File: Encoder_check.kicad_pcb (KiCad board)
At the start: 2 copper layers, 17.8 x 43.2 mm, 18 parts, among them J1 Conn_01x08, J2 Conn_01x06, P1 Digital, P2 Analog, P3 CONN_01X01, P4 CONN_01X01, P5 CONN_01X01, P6 CONN_01X01, U1 AM26LV32xD, U2 ST490AB

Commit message: AW
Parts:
- removed P3, P4, P5, P6: CONN_01X01, Socket_Arduino_Nano:1pin_Nano
- added C10: 10n, Capacitor_SMD:C_0603_1608Metric, F.Cu at (173.4, 63.7)
- added C11: DNP, Capacitor_SMD:C_0603_1608Metric, F.Cu at (173.4, 67.0)
- added C12: C, Capacitor_SMD:C_1206_3216Metric, B.Cu at (135.2, 85.1)
- added C13: 0.1u, Capacitor_SMD:C_0603_1608Metric, B.Cu at (139.9, 69.3)
- added C14: 3.3u, Capacitor_SMD:C_0805_2012Metric, B.Cu at (154.7, 55.4)
- added C15: 0.1u, Capacitor_SMD:C_0603_1608Metric, B.Cu at (148.5, 103.0)
- added C16: 1u, Capacitor_SMD:C_0805_2012Metric, B.Cu at (142.7, 104.8)
- added C17: C, Capacitor_SMD:C_0603_1608Metric, B.Cu at (151.0, 103.0)
- added C3: 220p, Capacitor_SMD:C_0603_1608Metric, B.Cu at (184.6, 75.1)
- added C4: 0.1u, Capacitor_SMD:C_0603_1608Metric, F.Cu at (184.8, 74.6)
- added C5: 220p, Capacitor_SMD:C_0603_1608Metric, B.Cu at (182.2, 98.4)
- added C6: 220p, Capacitor_SMD:C_0603_1608Metric, B.Cu at (182.2, 93.4)
- added C7: 0.1u, Capacitor_SMD:C_0603_1608Metric, B.Cu at (178.3, 106.3)
- added C8: C, Capacitor_SMD:C_0603_1608Metric, F.Cu at (170.6, 60.3)
- added C9: DNP, Capacitor_SMD:C_0603_1608Metric, F.Cu at (173.4, 60.4)
- added D10: LED, LED_SMD:LED_0603_1608Metric, F.Cu at (132.9, 61.4)
- added D11: LED, LED_SMD:LED_0603_1608Metric, F.Cu at (163.7, 114.6)
- added D4: D_TVS_x2_AAC, Package_TO_SOT_SMD:SOT-23, F.Cu at (175.9, 63.7)
- added D5: SK6805, LED_SMD:LED_SK6805_PLCC4_2.4x2.7mm_P1.3mm, F.Cu at (173.0, 115.0)
- added D6: SK6805, LED_SMD:LED_SK6805_PLCC4_2.4x2.7mm_P1.3mm, F.Cu at (178.2, 115.0)
- added D7: SK6805, LED_SMD:LED_SK6805_PLCC4_2.4x2.7mm_P1.3mm, F.Cu at (183.4, 115.0)
- added D8: D, Diode_SMD:D_SOD-523, B.Cu at (138.7, 91.4)
- added D9: D, Diode_SMD:D_SOD-523, B.Cu at (138.6, 87.0)
- added H1: MountingHole, MountingHole:MountingHole_3.2mm_M3, F.Cu at (132.2, 50.6)
- added H2: MountingHole, MountingHole:MountingHole_3.2mm_M3, F.Cu at (132.2, 115.6)
- added H3: MountingHole, MountingHole:MountingHole_3.2mm_M3, F.Cu at (190.2, 50.6)
- added H4: MountingHole, MountingHole:MountingHole_3.2mm_M3, F.Cu at (190.2, 115.6)
- added J3: Conn_01x04, Connector_JST:JST_EH_S4B-EH_1x04_P2.50mm_Horizontal, F.Cu at (136.1, 78.9)
- added J4: Screw_Terminal_01x06, TerminalBlock_TE-Connectivity:TerminalBlock_TE_282834-6_1x06_P2.54mm_Horizontal, F.Cu at (132.7, 83.9)
- added J5: Conn_01x02, Connector_PinHeader_2.54mm:PinHeader_1x02_P2.54mm_Vertical, F.Cu at (136.3, 66.9)
- added J6: Screw_Terminal_01x02, TerminalBlock_Phoenix:TerminalBlock_Phoenix_MKDS-1,5-2-5.08_1x02_P5.08mm_Horizontal, F.Cu at (188.0, 66.3)
- added J7: Barrel_Jack_Switch, Connector_BarrelJack:BarrelJack_Horizontal, F.Cu at (140.6, 61.6)
- added J8: Screw_Terminal_01x02, TerminalBlock_Phoenix:TerminalBlock_Phoenix_MKDS-1,5-2-5.08_1x02_P5.08mm_Horizontal, F.Cu at (134.0, 103.9)
- added J9: Screw_Terminal_01x04, TerminalBlock_TE-Connectivity:TerminalBlock_TE_282834-4_1x04_P2.54mm_Horizontal, F.Cu at (141.7, 115.1)
- added L1: L, Inductor_SMD:L_0603_1608Metric, F.Cu at (174.9, 67.0)
- added L2: L, Inductor_SMD:L_0603_1608Metric, F.Cu at (174.9, 60.4)
- added L3: L, Inductor_SMD:L_0603_1608Metric, B.Cu at (133.0, 81.8)
- added L4: L, Inductor_SMD:L_1210_3225Metric, B.Cu at (143.3, 108.9)
- added Q1: BSS138, Package_TO_SOT_SMD:SOT-23, B.Cu at (173.4, 115.0)
- added Q2: BSS138, Package_TO_SOT_SMD:SOT-23, B.Cu at (179.5, 77.1)
- added R10: 20k, Resistor_SMD:R_0603_1608Metric, B.Cu at (182.2, 94.8)
- added R11: 10k, Resistor_SMD:R_0603_1608Metric, B.Cu at (135.6, 88.5)
- added R12: 10k, Resistor_SMD:R_0603_1608Metric, B.Cu at (135.6, 89.9)
- added R13: 1k, Resistor_SMD:R_0603_1608Metric, B.Cu at (135.6, 92.6)
- added R14: 10k, Resistor_SMD:R_0603_1608Metric, B.Cu at (138.6, 88.5)
- added R15: 10k, Resistor_SMD:R_0603_1608Metric, B.Cu at (138.6, 89.9)
- added R16: R, Resistor_SMD:R_0603_1608Metric, B.Cu at (133.8, 69.9)
- added R17: 10k, Resistor_SMD:R_0603_1608Metric, B.Cu at (179.3, 74.3)
- added R18: 1k, Resistor_SMD:R_0603_1608Metric, B.Cu at (182.0, 77.2)
- added R19: 0.05, Inductor_SMD:L_0805_2012Metric, B.Cu at (145.8, 105.6)
- added R20: 0, Inductor_SMD:L_0805_2012Metric, B.Cu at (139.6, 106.0)
- added R21: R, Resistor_SMD:R_1206_3216Metric, B.Cu at (138.6, 108.9)
- added R22: R, Inductor_SMD:L_0603_1608Metric, B.Cu at (151.0, 106.0)
- added R23: 10k, Resistor_SMD:R_0603_1608Metric, B.Cu at (171.0, 115.0)
- added R24: 10k, Resistor_SMD:R_0603_1608Metric, B.Cu at (175.9, 115.0)
- added R25: 1k, Resistor_SMD:R_0603_1608Metric, B.Cu at (146.7, 112.9)
- added R26: R, Resistor_SMD:R_0603_1608Metric, B.Cu at (161.9, 112.2)
- added R27: R, Resistor_SMD:R_0603_1608Metric, F.Cu at (132.9, 58.3)
- added R28: R, Resistor_SMD:R_0603_1608Metric, F.Cu at (163.7, 113.0)
- added R4: 4.7k, Resistor_SMD:R_0603_1608Metric, B.Cu at (187.0, 78.7)
- added R5: 4.7k, Resistor_SMD:R_0603_1608Metric, B.Cu at (187.0, 80.1)
- added R6: 150, Resistor_SMD:R_0603_1608Metric, B.Cu at (187.0, 77.3)
- added R7: 150, Resistor_SMD:R_0603_1608Metric, B.Cu at (187.0, 75.9)
- added R8: 20k, Resistor_SMD:R_0603_1608Metric, B.Cu at (182.2, 104.8)
- added R9: 20k, Resistor_SMD:R_0603_1608Metric, B.Cu at (182.2, 99.8)
- added RN1: R_Pack02, Resistor_SMD:R_Array_Concave_2x0603, B.Cu at (183.0, 106.6)
- added RN2: R_Pack02, Resistor_SMD:R_Array_Concave_2x0603, B.Cu at (183.0, 101.6)
- added RN3: R_Pack02, Resistor_SMD:R_Array_Concave_2x0603, B.Cu at (183.0, 96.6)
- added RN4: R_Pack02, Resistor_SMD:R_Array_Concave_2x0603, F.Cu at (181.5, 104.3)
- added RN5: R_Pack02, Resistor_SMD:R_Array_Concave_2x0603, F.Cu at (181.5, 99.3)
- added RN6: R_Pack02, Resistor_SMD:R_Array_Concave_2x0603, F.Cu at (181.5, 94.3)
- added TC1: Thermocouple_PCB, Connector_Omega:Omega_PCC-SMP_1x2_P13.70mm_Horizontal, F.Cu at (174.9, 63.7)
- added U3: AM26LV32xD, Package_SO:SOIC-16_3.9x9.9mm_P1.27mm, B.Cu at (177.0, 100.4)
- added U4: SP3481CN, Package_SO:SOIC-8_3.9x4.9mm_P1.27mm, B.Cu at (141.1, 72.7)
- added U5: M78AR05-1, Converter_DCDC_my:Converter_DCDC_MINIMAX_M78AR05-1_THT, F.Cu at (152.2, 59.1)
- added U6: INA180A, Package_TO_SOT_SMD:SOT-23-5, B.Cu at (148.5, 105.6)
- added U7: A4953_LJ, Package_SO:SOIC-8-1EP_3.9x4.9mm_P1.27mm_EP2.41x3.3mm, B.Cu at (139.0, 101.3)
- added U8: TLP785, Package_DIP:DIP-4_W7.62mm, F.Cu at (152.4, 112.9)
- C1, C2: value C -> 220p; moved to B.Cu
- J1: value Conn_01x08 -> Conn_01x10; footprint TerminalBlock_TE-Connectivity:TerminalBlock_TE_282834-8_1x08_P2.54mm_Horizontal -> Connector_Multicomp:Multicomp_MC9A12-1034_2x05_P2.54mm_Vertical
- R1, R2, R3: moved to B.Cu
- U1: value AM26LV32xD -> MAX31855KASA; footprint Package_SO:SOIC-16_3.9x9.9mm_P1.27mm -> Package_SO:SOIC-8_3.9x4.9mm_P1.27mm; moved to F.Cu
- U2: value ST490AB -> ADM1491EBR; footprint Package_SO:SO-8_3.9x4.9mm_P1.27mm -> Package_SO:SOIC-14_3.9x8.7mm_P1.27mm
- moved J1 85.1 mm to (187.1, 96.0)
- moved J2 83.0 mm to (189.7, 88.1), turned to 90 degrees
- moved U2 68.1 mm to (180.4, 79.3)
- moved C2 65.8 mm to (184.6, 78.1), turned to 270 degrees
- moved D2 64.6 mm to (176.8, 95.5), turned to 270 degrees
- moved D1 63.5 mm to (179.3, 95.5), turned to 270 degrees
- moved R2 61.2 mm to (178.4, 92.8), turned to 90 degrees
- moved R1 59.2 mm to (179.9, 92.8), turned to 90 degrees
- moved C1 57.9 mm to (182.2, 103.4)
- moved D3 57.9 mm to (174.2, 95.5), turned to 270 degrees
- moved R3 57.1 mm to (176.9, 92.8), turned to 90 degrees
- moved U1 51.8 mm to (168.9, 63.7), turned to 180 degrees
- moved P1 16.1 mm to (155.5, 70.2)
- moved P2 16.1 mm to (170.8, 70.2)
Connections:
- C1 pad 1: +5V -> /inc_encoder/I_-
- C2 pad 1: +5V -> /ssi_encoder/Dout_-
- J1 pad 1: GND -> (no net)
- J1 pad 2: +5V -> GND
- J1 pad 3: Net-(J1-Pad3) -> +5V
- J1 pad 4: Net-(J1-Pad4) -> (no net)
- J1 pad 5: Net-(J1-Pad5) -> /inc_encoder/A+
- J1 pad 6: Net-(J1-Pad6) -> /inc_encoder/A-
- J1 pad 7: Net-(J1-Pad7) -> /inc_encoder/B+
- J1 pad 8: Net-(J1-Pad8) -> /inc_encoder/B-
- J2 pad 3: Net-(J2-Pad3) -> /ssi_encoder/C_-
- J2 pad 4: Net-(J2-Pad4) -> /ssi_encoder/C_+
- J2 pad 5: Net-(J2-Pad5) -> /ssi_encoder/D_-
- J2 pad 6: Net-(J2-Pad6) -> /ssi_encoder/D_+
- P1 pad 1: (no net) -> /1(Tx)
- P1 pad 12: (no net) -> /9(**)
- P1 pad 13: (no net) -> /10(**/SS)
- P1 pad 14: (no net) -> /11(**/MOSI)
- P1 pad 15: (no net) -> /12(MISO)
- P1 pad 2: (no net) -> /0(Rx)
- P1 pad 5: (no net) -> /2
- P1 pad 7: (no net) -> /4
- P1 pad 9: (no net) -> /6(**)
- P2 pad 14: (no net) -> +3V3
- P2 pad 6: (no net) -> /A6
- P2 pad 9: (no net) -> /A3
- U1 pad 1: Net-(J1-Pad4) -> GND
- U1 pad 2: Net-(J1-Pad3) -> Net-(C10-Pad2)
- U1 pad 3: /A0 -> Net-(C10-Pad1)
- U1 pad 4: /3(**) -> +3V3
- U1 pad 5: /A1 -> /A4
- U1 pad 6: Net-(J1-Pad5) -> /A3
- U1 pad 7: Net-(J1-Pad6) -> /12(MISO)
- U1 pad 8: GND -> (no net)
- U2 pad 1: +5V -> (no net)
- U2 pad 2: /A5 -> /12(MISO)
- U2 pad 3: /A4 -> Net-(Q2-Pad3)
- U2 pad 4: GND -> /3(**)
- U2 pad 5: Net-(J2-Pad3) -> /A4
- U2 pad 6: Net-(J2-Pad4) -> GND
- U2 pad 7: Net-(J2-Pad6) -> GND
- U2 pad 8: Net-(J2-Pad5) -> (no net)
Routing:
- net GND: track 0.00 -> 382.2 mm, vias 0 -> 8
- net +5V: track 0.00 -> 217.4 mm, vias 0 -> 5
- net +3V3: track 0.00 -> 162.7 mm, vias 0 -> 6
- net +24V: track 0.00 -> 88.2 mm, vias 0 -> 2
- net /12(MISO): track 0.00 -> 61.5 mm, vias 0 -> 2
- net /A4: track 0.00 -> 43.4 mm, vias 0 -> 2
- net /1(Tx): track 0.00 -> 41.1 mm, vias 0 -> 1
- net /A5: track 0.00 -> 39.2 mm, vias 0 -> 1
- net /A6: track 0.00 -> 31.7 mm, vias 0 -> 1
- net /A3: track 0.00 -> 31.3 mm
- net /3(**): track 0.00 -> 30.1 mm, vias 0 -> 2
- net /5(**): track 0.00 -> 29.2 mm, vias 0 -> 1
- net /4: track 0.00 -> 29.1 mm
- net /11(**/MOSI): track 0.00 -> 21.4 mm
- net /6(**): track 0.00 -> 21.0 mm
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- added copper zone on B.Cu, net GND
- added copper zone on F.Cu, net GND
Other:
- board size 17.8 x 43.2 mm -> 64 x 71 mm
- net class Default: clearance 0.2 -> 0.199; trace_width 0.25 -> 0.2
- rule trace_clearance: 0.2 -> 0.199
- rule trace_min: 0.2 -> 0.199
- board text added: "24V"
- board text added: "5V"
- board text added: "A"
- board text added: "Absolute Encoder"
- board text added: "B"
- board text added: "Brake"
- board text added: "D+"
- board text added: "D-"
- board text added: "GND"
- board text added: "I"
- board text added: "PULSE_OUT+"
- board text added: "PULSE_OUT-"
- board text added: "PWR+(24V)"
- board text added: "PWR-(0V)"
- board text added: "RS485"
- board text added: "SIG_GND"
- board text added: "SIG_OUT"
- board text added: "STO"
- board text added: "Term"
- board text added: "UTMII"

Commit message: これで発注
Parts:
- C16: footprint Capacitor_SMD:C_0805_2012Metric -> Capacitor_SMD:C_1206_3216Metric
- R28: moved to B.Cu
- moved R27 13.5 mm to (144.8, 64.6), turned to 0 degrees
- moved D10 9.27 mm to (141.6, 64.6), turned to 180 degrees
- moved Q2 7.00 mm to (175.3, 82.7)
- moved R17 6.68 mm to (175.1, 79.5)
- moved C4 5.26 mm to (179.9, 76.5), turned to 180 degrees
- moved R18 5.16 mm to (177.8, 80.2)
- moved C16 4.52 mm to (140.8, 100.7), turned to 90 degrees
- moved R19 4.44 mm to (143.2, 102.0)
- moved U6 4.44 mm to (145.9, 102.0)
- moved C15 4.44 mm to (145.9, 99.4)
- moved C17 4.44 mm to (148.4, 99.4)
- moved R22 4.44 mm to (148.4, 102.4)
- moved R26 3.69 mm to (165.0, 114.2), turned to 180 degrees
- moved R28 3.45 mm to (165.0, 116.2)
- moved U2 3.33 mm to (178.2, 81.8)
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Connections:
- J9 pad 1: +5V -> GND
- J9 pad 4: GND -> +5V
- R25 pad 2: Net-(J9-Pad2) -> Net-(J9-Pad3)
- U8 pad 2: Net-(J9-Pad3) -> Net-(J9-Pad2)
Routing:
- net +24V: track 88.2 -> 115.2 mm, vias 2 -> 4
- net GND: track 382.2 -> 371.0 mm, vias 8 -> 152
- net Net-(J9-Pad2): track 4.19 -> 13.7 mm
- net /5(**): track 29.2 -> 37.0 mm
- net /10(**/SS): track 19.7 -> 25.6 mm, vias 1 -> 0
- net /3(**): track 30.1 -> 24.2 mm
- net +5V: track 217.4 -> 223.2 mm, vias 5 -> 8
- net /A1: track 11.3 -> 16.4 mm
- net Net-(J9-Pad3): track 7.17 -> 2.21 mm
- net /A4: track 43.4 -> 38.6 mm, vias 2 -> 1
- net /11(**/MOSI): track 21.4 -> 24.9 mm
- net /12(MISO): track 61.5 -> 58.5 mm
- net /9(**): track 17.4 -> 20.1 mm
- net +3V3: track 162.7 -> 160.1 mm, vias 6 -> 5
- net /ssi_encoder/Dout_-: track 6.46 -> 8.33 mm
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- added copper zone on F.Cu, net /thermocouple/T+
- added copper zone on F.Cu, net /thermocouple/T-
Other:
- board text added: "C+"
- board text added: "C-"
- board text removed: "Absolute Encoder"

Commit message: 見つけた設計ミスを全部反映
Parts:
- removed R1, R2, R3: R, Resistor_SMD:R_0603_1608Metric
- added L5: L, Inductor_SMD:L_0603_1608Metric, F.Cu at (171.3, 58.0)
- added L6: L, Inductor_SMD:L_0603_1608Metric, B.Cu at (146.6, 97.1)
- added R29: 10k, Resistor_SMD:R_0603_1608Metric, F.Cu at (182.6, 94.5)
- added R30: 20k, Resistor_SMD:R_0603_1608Metric, F.Cu at (181.0, 94.5)
- C17, C8: value C -> 0.1u
- J1: value Conn_01x10 -> Conn_02x05_Odd_Even
- J2: value Conn_01x06 -> Screw_Terminal_01x06
- R16: value R -> 120
- R27: value R -> 20k
- R4: value 4.7k -> 10k; moved to F.Cu
- R5: value 4.7k -> 20k; moved to F.Cu
- R6: value 150 -> 10k; moved to F.Cu
- R7: value 150 -> 20k; moved to F.Cu
- RN1, RN2, RN3: value R_Pack02 -> 150
- RN4: value R_Pack02 -> 4.7k; moved to B.Cu
- RN5: value R_Pack02 -> 150; moved to B.Cu
- RN6: value R_Pack02 -> 1k; footprint Resistor_SMD:R_Array_Concave_2x0603 -> Resistor_SMD:R_Array_Concave_4x0603; moved to B.Cu
- U2: value ADM1491EBR -> ISL83491
- U4: value SP3481CN -> ST485BDR
- moved R5 26.0 mm to (181.0, 104.5), turned to 270 degrees
- moved RN4 25.7 mm to (184.9, 78.8), turned to 180 degrees
- moved R4 24.3 mm to (182.6, 104.5), turned to 270 degrees
- moved R7 23.9 mm to (181.0, 99.5), turned to 270 degrees
- moved RN5 23.0 mm to (184.9, 76.6), turned to 0 degrees
- moved R6 22.3 mm to (182.6, 99.5), turned to 270 degrees
- moved RN6 4.39 mm to (178.5, 91.1)
- moved C4 1.53 mm to (181.2, 75.7), turned to 90 degrees
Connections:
- C15 pad 1: +3V3 -> Net-(C15-Pad1)
- C4 pad 1: +5V -> +3V3
- C7 pad 1: +5V -> +3V3
- C8 pad 1: +3V3 -> Net-(C8-Pad1)
- R17 pad 2: +5V -> +3V3
- R4 pad 1: /ssi_encoder/D_- -> +3V3
- R4 pad 2: +3V3 -> /inc_encoder/I_+
- R5 pad 1: GND -> +3V3
- R5 pad 2: /ssi_encoder/D_- -> /inc_encoder/I_-
- R6 pad 1: /ssi_encoder/Dout_- -> +3V3
- R6 pad 2: /ssi_encoder/D_- -> /inc_encoder/B_+
- R7 pad 1: /ssi_encoder/Dout_+ -> +3V3
- R7 pad 2: /ssi_encoder/D_+ -> /inc_encoder/B_-
- RN4 pad 1: /inc_encoder/I_- -> /ssi_encoder/D_-
- RN4 pad 2: /inc_encoder/I_+ -> /ssi_encoder/D_-
- RN4 pad 4: +3V3 -> GND
- RN5 pad 1: /inc_encoder/B_- -> /ssi_encoder/Dout_-
- RN5 pad 2: /inc_encoder/B_+ -> /ssi_encoder/Dout_+
- RN5 pad 3: +3V3 -> /ssi_encoder/D_+
- RN5 pad 4: +3V3 -> /ssi_encoder/D_-
- RN6 pad 1: /inc_encoder/A_- -> Net-(D1-Pad1)
- RN6 pad 2: /inc_encoder/A_+ -> Net-(D2-Pad1)
- RN6 pad 3: +3V3 -> Net-(D3-Pad1)
- RN6 pad 4: +3V3 -> (no net)
- U1 pad 4: +3V3 -> Net-(C8-Pad1)
- U2 pad 13: +5V -> +3V3
- U2 pad 14: +5V -> +3V3
- U3 pad 12: +5V -> +3V3
- U3 pad 16: +5V -> +3V3
- U6 pad 5: +3V3 -> Net-(C15-Pad1)
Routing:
- net +3V3: track 160.1 -> 199.9 mm, vias 5 -> 8
- net +5V: track 223.2 -> 196.8 mm, vias 8 -> 6
- net GND: track 371.0 -> 359.4 mm, vias 152 -> 163
- net Net-(C15-Pad1): track 0.00 -> 3.12 mm
- net Net-(C8-Pad1): track 0.00 -> 3.05 mm
- net Net-(D3-Pad1): track 3.41 -> 5.29 mm
- net Net-(D1-Pad1): track 1.82 -> 3.42 mm
- net Net-(D2-Pad1): track 2.13 -> 3.28 mm
- net /ssi_encoder/D_-: track 5.19 -> 4.36 mm
- net /ssi_encoder/Dout_+: track 8.67 -> 7.84 mm
- net /12(MISO): track 58.5 -> 59.3 mm
- net /3(**): track 24.2 -> 23.4 mm
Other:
- rule trace_min: 0.199 -> 0.2

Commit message: 部品のパラメータ未記入部分があったので追記
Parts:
- removed D11: LED, LED_SMD:LED_0603_1608Metric
- removed R28: R, Resistor_SMD:R_0603_1608Metric
- added R1: 1k, Resistor_SMD:R_0603_1608Metric, B.Cu at (163.4, 115.0)
- R26: value R -> 10k
- moved C14 2.90 mm to (155.2, 52.0)
- moved U5 2.90 mm to (152.2, 56.2)
- moved R26 0.80 mm to (165.0, 115.0), turned to 270 degrees
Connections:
- R26 pad 2: /10(**/SS) -> Net-(R1-Pad2)
- U8 pad 4: /10(**/SS) -> Net-(R1-Pad2)
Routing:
- net GND: track 359.4 -> 348.9 mm, vias 163 -> 160
- net Net-(R1-Pad2): track 0.00 -> 4.29 mm
- net /10(**/SS): track 25.6 -> 21.5 mm
- net Net-(D11-Pad1): track 2.03 -> 0.00 mm, vias 1 -> 0
- net +24V: track 115.2 -> 117.2 mm
- net +5V: track 196.8 -> 198.0 mm
- net /brake/brake_-: track 3.17 -> 3.76 mm

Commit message: エンコーダの配線ミスってた
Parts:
- R21: value R -> 0
- R22: value R -> 100
- moved C1 5.00 mm to (182.2, 108.4)
- moved R8 5.00 mm to (182.2, 109.8)
- moved R5 4.51 mm to (182.6, 108.7), turned to 90 degrees
- moved R4 4.49 mm to (181.0, 108.7), turned to 90 degrees
- moved R29 3.85 mm to (180.6, 97.8), turned to 90 degrees
- moved R30 3.67 mm to (182.6, 97.8), turned to 90 degrees
- moved R6 2.41 mm to (180.6, 100.9)
- moved R9 2.09 mm to (183.8, 101.2)
- moved C5 2.09 mm to (183.8, 99.8)
- moved R7 2.09 mm to (182.6, 100.9)
- moved RN2 1.35 mm to (183.0, 103.0)
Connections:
- J1 pad 10: /inc_encoder/I- -> /inc_encoder/I+
- J1 pad 2: GND -> +5V
- J1 pad 3: +5V -> GND
- J1 pad 5: /inc_encoder/A+ -> /inc_encoder/A-
- J1 pad 6: /inc_encoder/A- -> /inc_encoder/A+
- J1 pad 7: /inc_encoder/B+ -> /inc_encoder/B-
- J1 pad 8: /inc_encoder/B- -> /inc_encoder/B+
- J1 pad 9: /inc_encoder/I+ -> /inc_encoder/I-
- RN2 pad 1: /inc_encoder/B_+ -> /inc_encoder/B_-
- RN2 pad 2: /inc_encoder/B_- -> /inc_encoder/B_+
- RN2 pad 3: /inc_encoder/B- -> /inc_encoder/B+
- RN2 pad 4: /inc_encoder/B+ -> /inc_encoder/B-
- U3 pad 13: (no net) -> /A1
- U3 pad 14: (no net) -> /inc_encoder/B_+
- U3 pad 15: (no net) -> /inc_encoder/B_-
- U3 pad 5: /A1 -> (no net)
- U3 pad 6: /inc_encoder/B_+ -> (no net)
- U3 pad 7: /inc_encoder/B_- -> (no net)
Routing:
- net GND: track 348.9 -> 284.1 mm, vias 160 -> 164
- net +3V3: track 200.3 -> 182.5 mm, vias 8 -> 9
- net /inc_encoder/B_+: track 11.9 -> 4.02 mm, vias 2 -> 1
- net /A1: track 16.4 -> 21.8 mm
- net +5V: track 198.0 -> 202.1 mm
- net /inc_encoder/B_-: track 13.6 -> 9.59 mm, vias 2 -> 1
- net /inc_encoder/A+: track 8.08 -> 11.5 mm, vias 0 -> 1
- net /inc_encoder/I_-: track 17.1 -> 20.1 mm
- net /inc_encoder/A-: track 8.88 -> 11.5 mm, vias 0 -> 1
- net /inc_encoder/A_+: track 5.51 -> 3.85 mm
- net Net-(D2-Pad1): track 3.28 -> 4.88 mm
- net /inc_encoder/I_+: track 16.2 -> 14.8 mm
- net /inc_encoder/I+: track 6.92 -> 6.41 mm
- net /inc_encoder/I-: track 6.92 -> 6.41 mm
- added copper zone on F.Cu, net +24V

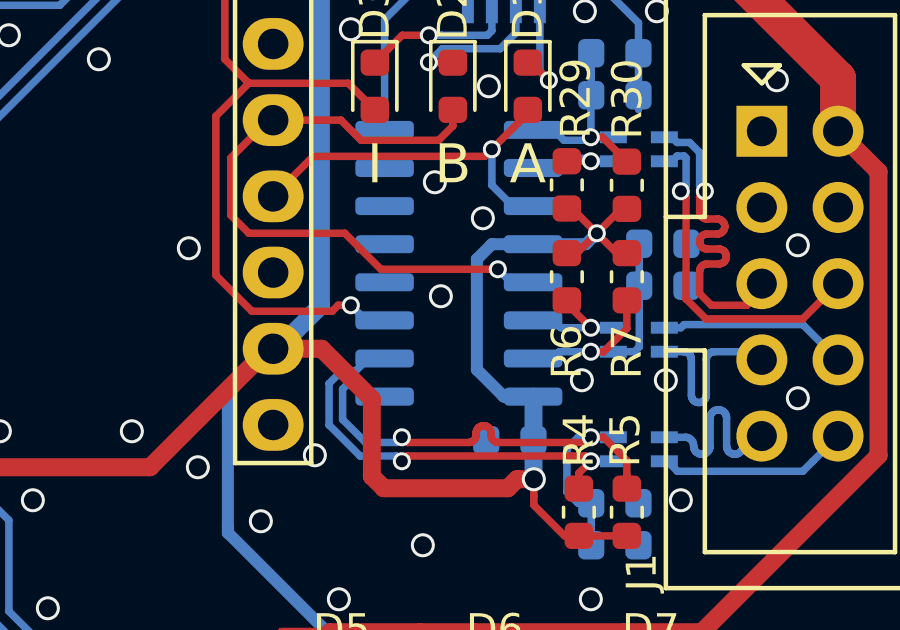
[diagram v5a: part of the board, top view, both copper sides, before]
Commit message: レシーバの出力が有効になっていないとうアホなミスを修正
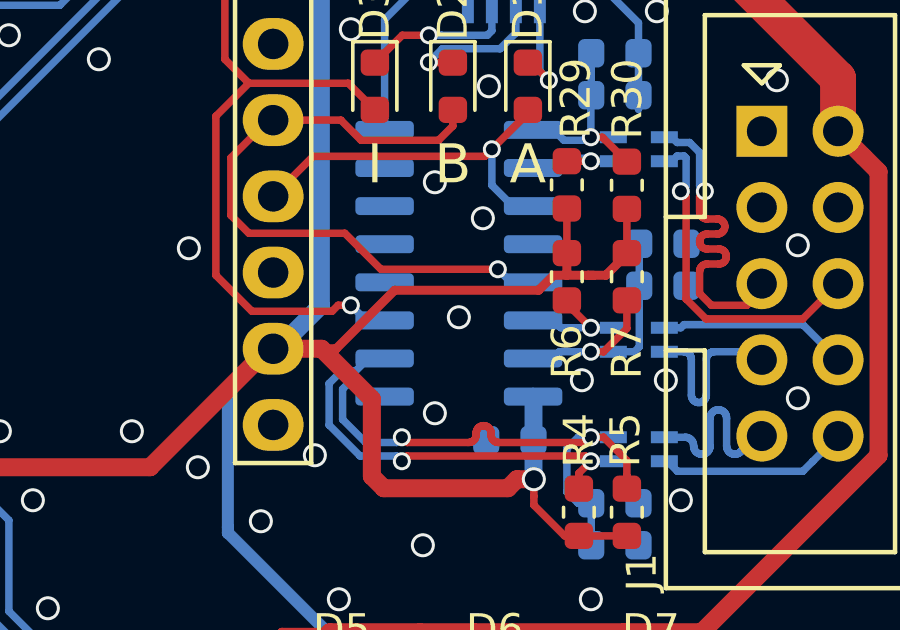
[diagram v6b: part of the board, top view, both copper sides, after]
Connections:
- U3 pad 12: +3V3 -> GND
- U3 pad 4: (no net) -> GND
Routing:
- net +3V3: track 182.5 -> 185.1 mm, vias 9 -> 8
- net GND: vias 164 -> 165

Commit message: 設計修正
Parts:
- removed R21: 0, Resistor_SMD:R_1206_3216Metric
- added J10: Conn_01x02, Connector_Amass:XT30PB, F.Cu at (132.0, 59.9)
- added L7: L, Inductor_SMD:L_1210_3225Metric, B.Cu at (139.0, 109.4)
- added R2: 10k, Resistor_SMD:R_0603_1608Metric, B.Cu at (135.6, 91.5)
- moved C14 22.4 mm to (144.1, 71.4), turned to 90 degrees
- moved U5 15.5 mm to (141.7, 67.6), turned to 270 degrees
- moved C13 11.4 mm to (143.7, 80.0), turned to 270 degrees
- moved R27 10.7 mm to (137.0, 57.3), turned to 90 degrees
- moved U4 8.54 mm to (140.3, 81.2), turned to 90 degrees
- moved L5 7.02 mm to (164.6, 60.1), turned to 0 degrees
- moved D10 6.23 mm to (137.0, 60.4), turned to 270 degrees
- moved C5 4.60 mm to (179.2, 99.8)
- moved D1 4.60 mm to (174.7, 94.5)
- moved D2 4.60 mm to (172.2, 94.5)
- moved J6 4.60 mm to (183.4, 66.3)
- moved Q2 4.60 mm to (170.7, 82.7)
- moved R18 4.60 mm to (173.2, 80.2)
- moved R9 4.60 mm to (179.2, 101.2)
- moved C1 4.60 mm to (177.6, 108.4)
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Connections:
- R12 pad 1: Net-(R11-Pad2) -> /utm/SIG_OUT
- R12 pad 2: /utm/SIG_OUT -> Net-(R11-Pad2)
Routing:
- net +5V: track 202.1 -> 157.5 mm, vias 6 -> 4
- net +24V: track 117.2 -> 87.7 mm
- net +3V3: track 185.1 -> 173.2 mm, vias 8 -> 6
- net /0(Rx): track 12.8 -> 21.0 mm, vias 0 -> 1
- net GND: track 284.1 -> 291.5 mm, vias 165 -> 182
- net /rs485/RS485_+: track 8.60 -> 15.5 mm
- net /rs485/RS485_-: track 8.23 -> 15.1 mm
- net /9(**): track 20.1 -> 14.5 mm
- net /A6: track 33.4 -> 28.0 mm
- net /A5: track 39.3 -> 34.9 mm
- net /6(**): track 21.9 -> 17.7 mm
- net /10(**/SS): track 21.5 -> 24.9 mm
- net /4: track 29.2 -> 26.8 mm
- net /2: track 17.1 -> 14.8 mm, vias 0 -> 1
- net /1(Tx): track 42.6 -> 40.5 mm
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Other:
- board size 64 x 71 mm -> 60 x 71 mm
- rule trace_min: 0.2 -> 0
- board text removed: "Term"
